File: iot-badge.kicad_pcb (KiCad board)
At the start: 2 copper layers, 70 x 100 mm, 38 parts, among them J1 USB_C_Receptacle_USB2.0, Q1 BC847, Q2 BC847, SW1 SW_Push, SW2 SW_Push, SW3 SW_Push, SW4 SW_Push, SW5 SW_Push, SW6 SW_Push, SW7 E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

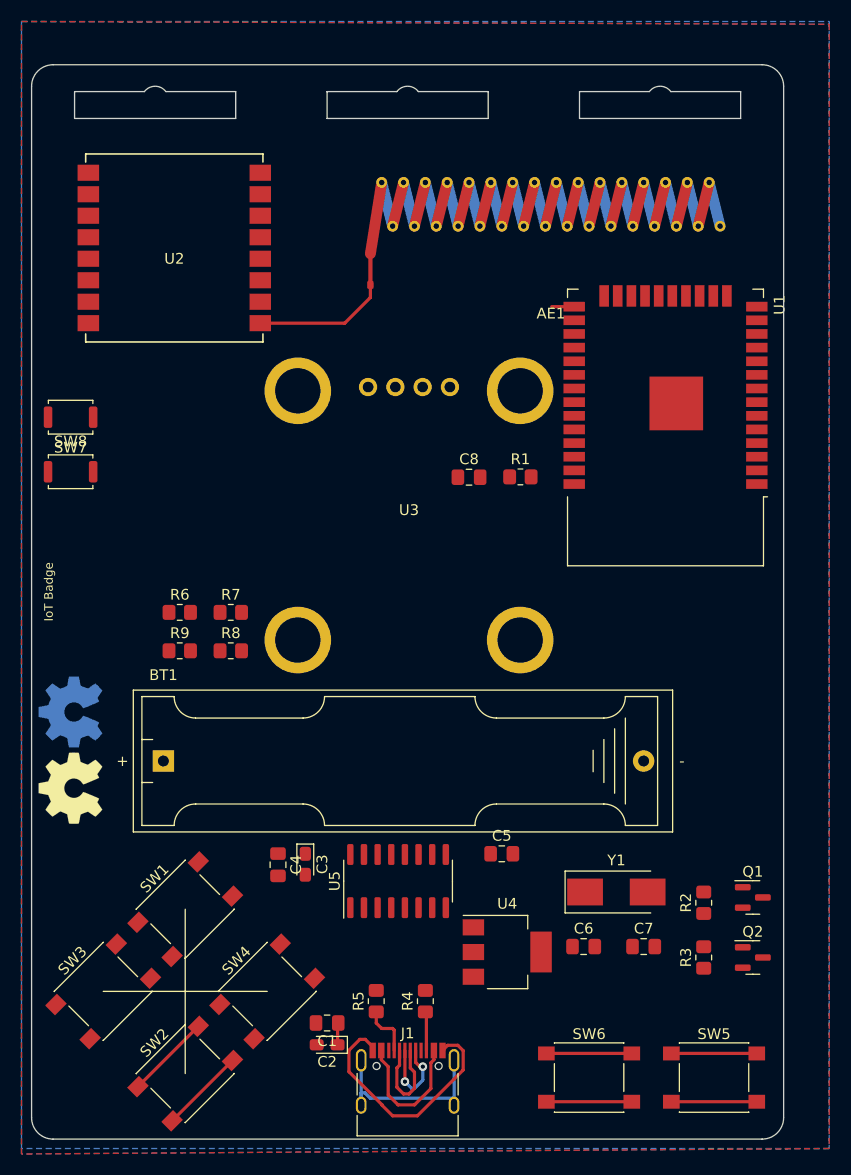
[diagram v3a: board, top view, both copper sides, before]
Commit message: added crystal and led rgb
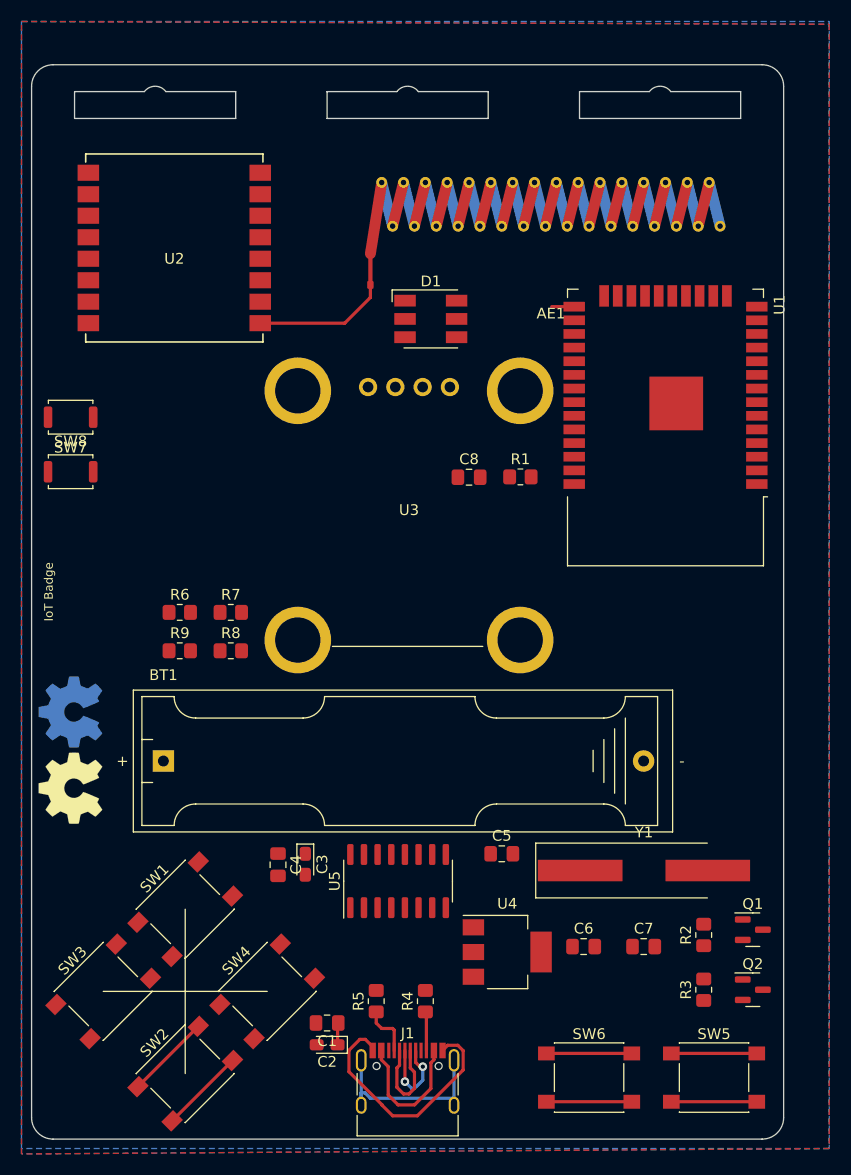
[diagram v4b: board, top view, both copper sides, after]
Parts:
- added D1: LED_RGB, LED_SMD:LED_RGB_5050-6, F.Cu at (137.2, 73.7)
- Y1: footprint Crystal:Crystal_SMD_0603-2Pin_6.0x3.5mm_HandSoldering -> Crystal:Crystal_SMD_HC49-SD_HandSoldering
- moved Y1 3.25 mm to (157.0, 125.0)
- moved Q1 3.00 mm to (167.1, 130.5)
- moved Q2 3.00 mm to (167.1, 136.1)
- moved R2 3.00 mm to (162.6, 131.0)
- moved R3 3.00 mm to (162.6, 136.1)

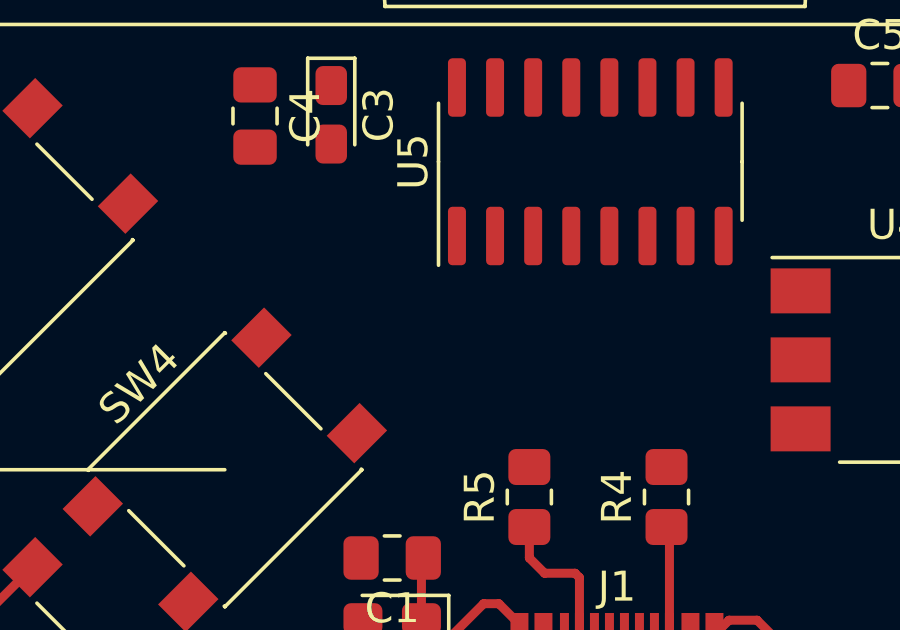
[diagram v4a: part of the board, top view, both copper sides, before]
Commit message: diode added to power
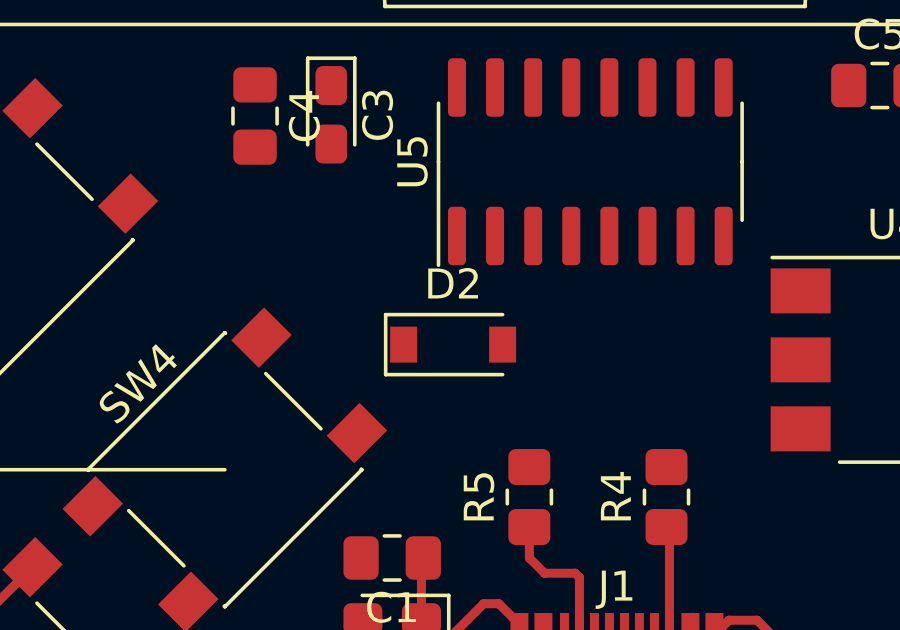
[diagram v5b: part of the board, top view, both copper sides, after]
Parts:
- added D2: D_Schottky, Diode_SMD:D_SOD-123, F.Cu at (129.5, 132.1)
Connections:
- J1 pad A4: Net-(C1-Pad1) -> Net-(J1-PadA4)
- J1 pad A9: Net-(C1-Pad1) -> Net-(J1-PadA4)
- J1 pad B4: Net-(C1-Pad1) -> Net-(J1-PadA4)
- J1 pad B9: Net-(C1-Pad1) -> Net-(J1-PadA4)
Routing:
- net Net-(C1-Pad1): track 15.3 -> 2.21 mm
- net Net-(J1-PadA4): track 0.00 -> 13.1 mm
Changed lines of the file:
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@@
   (net 80 "unconnected-(D1-Pad5)")
   (net 81 "unconnected-(D1-Pad6)")
+  (net 82 "Net-(J1-PadA4)")
   (footprint "Symbol:OSHW-Symbol_6.7x6mm_SilkScreen" (layer "F.Cu")
     (at 103.632 117.348 90)
@@
       ) (layer "F.SilkS") (width 0.01) (fill solid))
   )
+  (footprint "Diode_SMD:D_SOD-123" (layer "F.Cu")
+    (at 129.54 132.08)
+    (descr "SOD-123")
+    (tags "SOD-123")
+    (property "Sheetfile" "iot-badge.kicad_sch")
+    (property "Sheetname" "")
+    (attr smd)
+    (fp_text reference "D2" (at 0 -2) (layer "F.SilkS")
+      (effects (font (size 1 1) (thickness 0.15)))
+    )
+    (fp_text value "D_Schottky" (at 0 2.1) (layer "F.Fab")
+      (effects (font (size 1 1) (thickness 0.15)))
+    )
+    (fp_text user "${REFERENCE}" (at 0 -2) (layer "F.Fab")
+      (effects (font (size 1 1) (thickness 0.15)))
+    )
+    (fp_line (start -2.25 -1) (end -2.25 1) (layer "F.SilkS") (width 0.12))
+    (fp_line (start -2.25 1) (end 1.65 1) (layer "F.SilkS") (width 0.12))
+    (fp_line (start -2.25 -1) (end 1.65 -1) (layer "F.SilkS") (width 0.12))
+    (fp_line (start -2.35 -1.15) (end -2.35 1.15) (layer "F.CrtYd") (width 0.05))
+    (fp_line (start -2.35 -1.15) (end 2.35 -1.15) (layer "F.CrtYd") (width 0.05))
+    (fp_line (start 2.35 -1.15) (end 2.35 1.15) (layer "F.CrtYd") (width 0.05))
+    (fp_line (start 2.35 1.15) (end -2.35 1.15) (layer "F.CrtYd") (width 0.05))
+    (fp_line (start -1.4 -0.9) (end 1.4 -0.9) (layer "F.Fab") (width 0.1))
+    (fp_line (start -1.4 0.9) (end -1.4 -0.9) (layer "F.Fab") (width 0.1))
+    (fp_line (start -0.35 0) (end -0.35 0.55) (layer "F.Fab") (width 0.1))
+    (fp_line (start 1.4 -0.9) (end 1.4 0.9) (layer "F.Fab") (width 0.1))
+    (fp_line (start -0.75 0) (end -0.35 0) (layer "F.Fab") (width 0.1))
+    (fp_line (start 0.25 0.4) (end -0.35 0) (layer "F.Fab") (width 0.1))
+    (fp_line (start 1.4 0.9) (end -1.4 0.9) (layer "F.Fab") (width 0.1))
+    (fp_line (start 0.25 -0.4) (end 0.25 0.4) (layer "F.Fab") (width 0.1))
+    (fp_line (start 0.25 0) (end 0.75 0) (layer "F.Fab") (width 0.1))
+    (fp_line (start -0.35 0) (end 0.25 -0.4) (layer "F.Fab") (width 0.1))
+    (fp_line (start -0.35 0) (end -0.35 -0.55) (layer "F.Fab") (width 0.1))
+    (pad "1" smd rect (at -1.65 0) (size 0.9 1.2) (layers "F.Cu" "F.Paste" "F.Mask")
+      (net 13 "Net-(C1-Pad1)") (pinfunction "K") (pintype "passive"))
+    (pad "2" smd rect (at 1.65 0) (size 0.9 1.2) (layers "F.Cu" "F.Paste" "F.Mask")
+      (net 82 "Net-(J1-PadA4)") (pinfunction "A") (pintype "passive"))
+    (model "${KICAD6_3DMODEL_DIR}/Diode_SMD.3dshapes/D_SOD-123.wrl"
+      (offset (xyz 0 0 0))
+      (scale (xyz 1 1 1))
+      (rotate (xyz 0 0 0))
+    )
+  )
   (footprint "RF_PCB_Antenna:Micrel_Heli_2" (layer "F.Cu")
     (at 148.336 62.992)
@@
       (net 57 "Earth") (pinfunction "GND") (pintype "passive"))
     (pad "A4" smd rect (at -2.45 -4.045) (size 0.6 1.45) (layers "F.Cu" "F.Paste" "F.Mask")
-      (net 13 "Net-(C1-Pad1)") (pinfunction "VBUS") (pintype "passive"))
+      (net 82 "Net-(J1-PadA4)") (pinfunction "VBUS") (pintype "passive"))
     (pad "A5" smd rect (at -1.25 -4.045) (size 0.3 1.45) (layers "F.Cu" "F.Paste" "F.Mask")
       (net 58 "Net-(J1-PadA5)") (pinfunction "CC1") (pintype "bidirectional"))
@@
       (net 59 "unconnected-(J1-PadA8)") (pinfunction "SBU1") (pintype "bidirectional+no_connect"))
     (pad "A9" smd rect (at 2.45 -4.045) (size 0.6 1.45) (layers "F.Cu" "F.Paste" "F.Mask")
-      (net 13 "Net-(C1-Pad1)") (pinfunction "VBUS") (pintype "passive"))
+      (net 82 "Net-(J1-PadA4)") (pinfunction "VBUS") (pintype "passive"))
     (pad "A12" smd rect (at 3.25 -4.045) (size 0.6 1.45) (layers "F.Cu" "F.Paste" "F.Mask")
       (net 57 "Earth") (pinfunction "GND") (pintype "passive"))
@@
       (net 57 "Earth") (pinfunction "GND") (pintype "passive"))
     (pad "B4" smd rect (at 2.45 -4.045) (size 0.6 1.45) (layers "F.Cu" "F.Paste" "F.Mask")
-      (net 13 "Net-(C1-Pad1)") (pinfunction "VBUS") (pintype "passive"))
+      (net 82 "Net-(J1-PadA4)") (pinfunction "VBUS") (pintype "passive"))
     (pad "B5" smd rect (at 1.75 -4.045) (size 0.3 1.45) (layers "F.Cu" "F.Paste" "F.Mask")
       (net 60 "Net-(J1-PadB5)") (pinfunction "CC2") (pintype "bidirectional"))
@@
       (net 61 "unconnected-(J1-PadB8)") (pinfunction "SBU2") (pintype "bidirectional+no_connect"))
     (pad "B9" smd rect (at -2.45 -4.045) (size 0.6 1.45) (layers "F.Cu" "F.Paste" "F.Mask")
-      (net 13 "Net-(C1-Pad1)") (pinfunction "VBUS") (pintype "passive"))
+      (net 82 "Net-(J1-PadA4)") (pinfunction "VBUS") (pintype "passive"))
     (pad "B12" smd rect (at -3.25 -4.045) (size 0.6 1.45) (layers "F.Cu" "F.Paste" "F.Mask")
       (net 57 "Earth") (pinfunction "GND") (pintype "passive"))
@@
   (segment (start 147.917 142.022) (end 155.867 142.022) (width 0.3) (layer "F.Cu") (net 11))
   (segment (start 155.867 146.522) (end 147.917 146.522) (width 0.3) (layer "F.Cu") (net 12))
-  (segment (start 137.165 142.896) (end 137.45 142.611) (width 0.3) (layer "F.Cu") (net 13))
-  (segment (start 134.112 146.812) (end 135.646 146.812) (width 0.3) (layer "F.Cu") (net 13))
-  (segment (start 137.45 142.611) (end 137.45 141.751) (width 0.3) (layer "F.Cu") (net 13))
-  (segment (start 135.646 146.812) (end 137.165 145.294) (width 0.3) (layer "F.Cu") (net 13))
-  (segment (start 132.55 142.611) (end 133.195 143.256) (width 0.3) (layer "F.Cu") (net 13))
   (segment (start 128.483 141.224) (end 128.483 139.2545) (width 0.3) (layer "F.Cu") (net 13))
-  (segment (start 137.165 145.294) (end 137.165 142.896) (width 0.3) (layer "F.Cu") (net 13))
-  (segment (start 133.195 143.256) (end 133.195 145.895) (width 0.3) (layer "F.Cu") (net 13))
-  (segment (start 133.195 145.895) (end 134.112 146.812) (width 0.3) (layer "F.Cu") (net 13))
   (segment (start 128.483 139.2545) (end 128.5455 139.192) (width 0.3) (layer "F.Cu") (net 13))
   (segment (start 128.6498 139.0877) (end 128.5455 139.192) (width 0.3) (layer "F.Cu") (net 13))
-  (segment (start 132.55 141.751) (end 132.55 142.611) (width 0.3) (layer "F.Cu") (net 13))
   (segment (start 121.284 74.056) (end 129.144 74.056) (width 0.3) (layer "F.Cu") (net 49))
   (segment (start 131.536 71.664) (end 131.536 70.842) (width 0.3) (layer "F.Cu") (net 49))
@@
   (segment (start 135.25 143.378) (end 135.636 143.764) (width 0.3) (layer "F.Cu") (net 72))
   (segment (start 150.504 72.517) (end 148.4094 72.517) (width 0.3) (layer "F.Cu") (net 75))
+  (segment (start 137.165 142.896) (end 137.45 142.611) (width 0.3) (layer "F.Cu") (net 82))
+  (segment (start 134.112 146.812) (end 135.646 146.812) (width 0.3) (layer "F.Cu") (net 82))
+  (segment (start 137.45 142.611) (end 137.45 141.751) (width 0.3) (layer "F.Cu") (net 82))
+  (segment (start 135.646 146.812) (end 137.165 145.294) (width 0.3) (layer "F.Cu") (net 82))
+  (segment (start 132.55 142.611) (end 133.195 143.256) (width 0.3) (layer "F.Cu") (net 82))
+  (segment (start 137.165 145.294) (end 137.165 142.896) (width 0.3) (layer "F.Cu") (net 82))
+  (segment (start 133.195 143.256) (end 133.195 145.895) (width 0.3) (layer "F.Cu") (net 82))
+  (segment (start 133.195 145.895) (end 134.112 146.812) (width 0.3) (layer "F.Cu") (net 82))
+  (segment (start 132.55 141.751) (end 132.55 142.611) (width 0.3) (layer "F.Cu") (net 82))
   (zone (net 57) (net_name "Earth") (layers F&B.Cu) (hatch edge 0.508)
     (connect_pads (clearance 0.508))

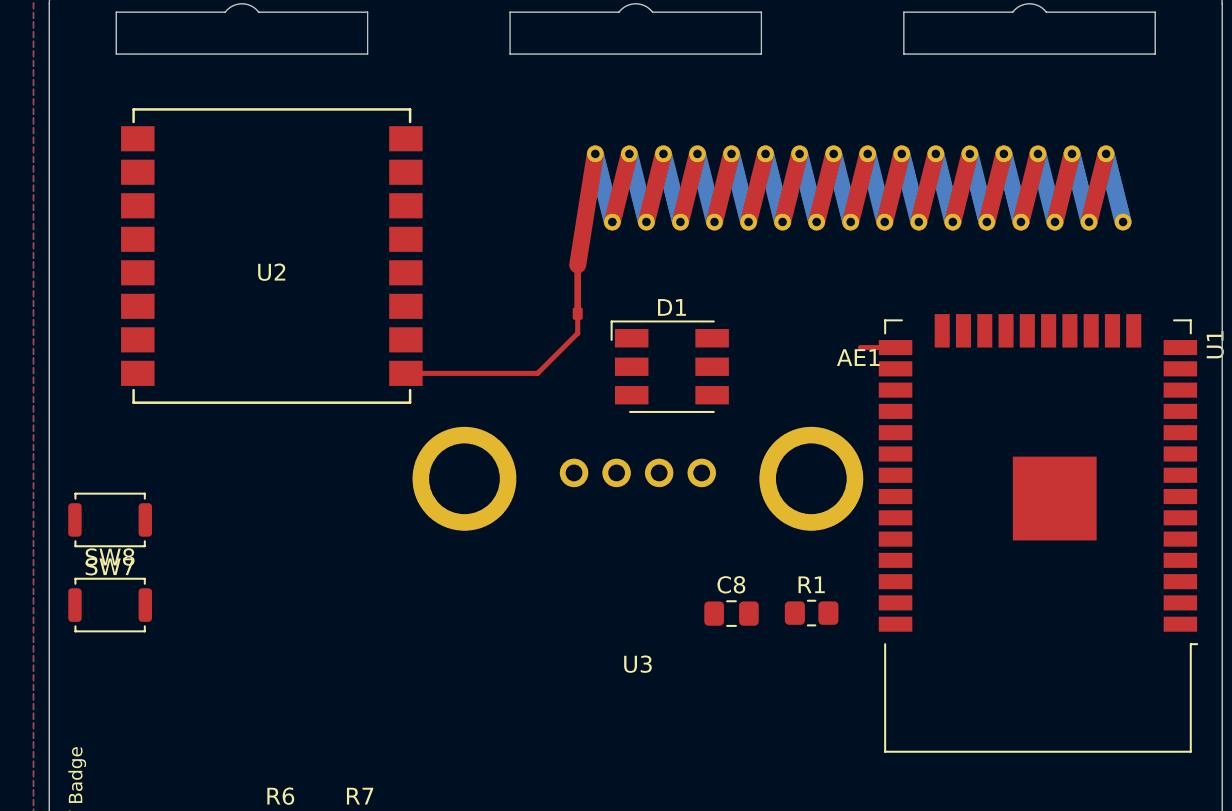
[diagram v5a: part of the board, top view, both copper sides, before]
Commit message: added external ant
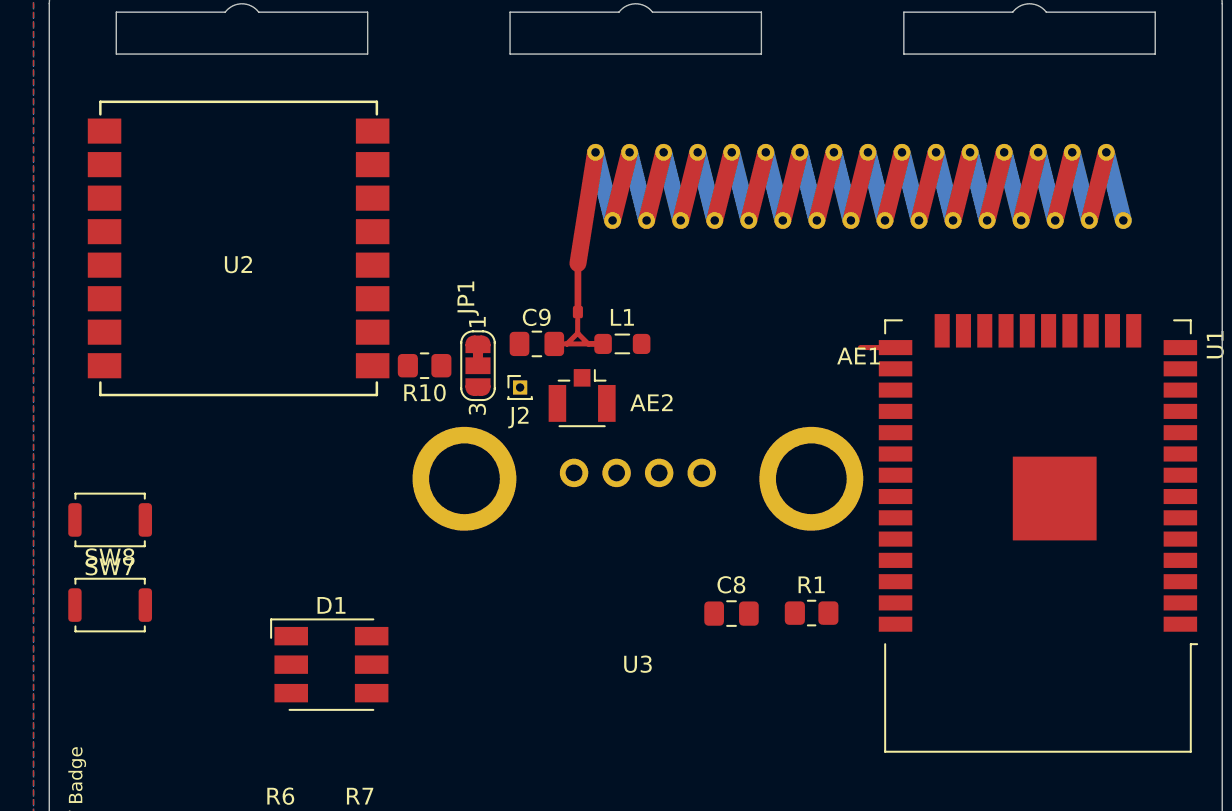
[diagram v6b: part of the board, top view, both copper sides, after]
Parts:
- added AE2: EXT U.FL, Connector_Coaxial:U.FL_Hirose_U.FL-R-SMT-1_Vertical, F.Cu at (131.8, 75.4)
- added C9: C, Capacitor_SMD:C_0805_2012Metric_Pad1.18x1.45mm_HandSolder, F.Cu at (129.1, 72.3)
- added J2: Conn_01x01_Male, Connector_PinHeader_1.00mm:PinHeader_1x01_P1.00mm_Vertical, F.Cu at (128.1, 74.9)
- added JP1: Jumper_3_Bridged12, Jumper:SolderJumper-3_P1.3mm_Bridged12_RoundedPad1.0x1.5mm_NumberLabels, F.Cu at (125.6, 73.6)
- added L1: L, Inductor_SMD:L_0805_2012Metric_Pad1.05x1.20mm_HandSolder, F.Cu at (134.2, 72.3)
- added R10: R, Resistor_SMD:R_0805_2012Metric_Pad1.20x1.40mm_HandSolder, F.Cu at (122.4, 73.6)
- moved D1 27.0 mm to (116.8, 91.4)
- moved U2 2.04 mm to (111.3, 66.6)
- moved AE1 0.09 mm to (148.3, 62.9)
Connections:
- U2 pad 1: Net-(AE1-Pad1) -> Net-(U2-Pad1)
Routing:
- net Net-(AE1-Pad1): track 12.1 -> 6.41 mm
